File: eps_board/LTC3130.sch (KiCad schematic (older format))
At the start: 13 parts

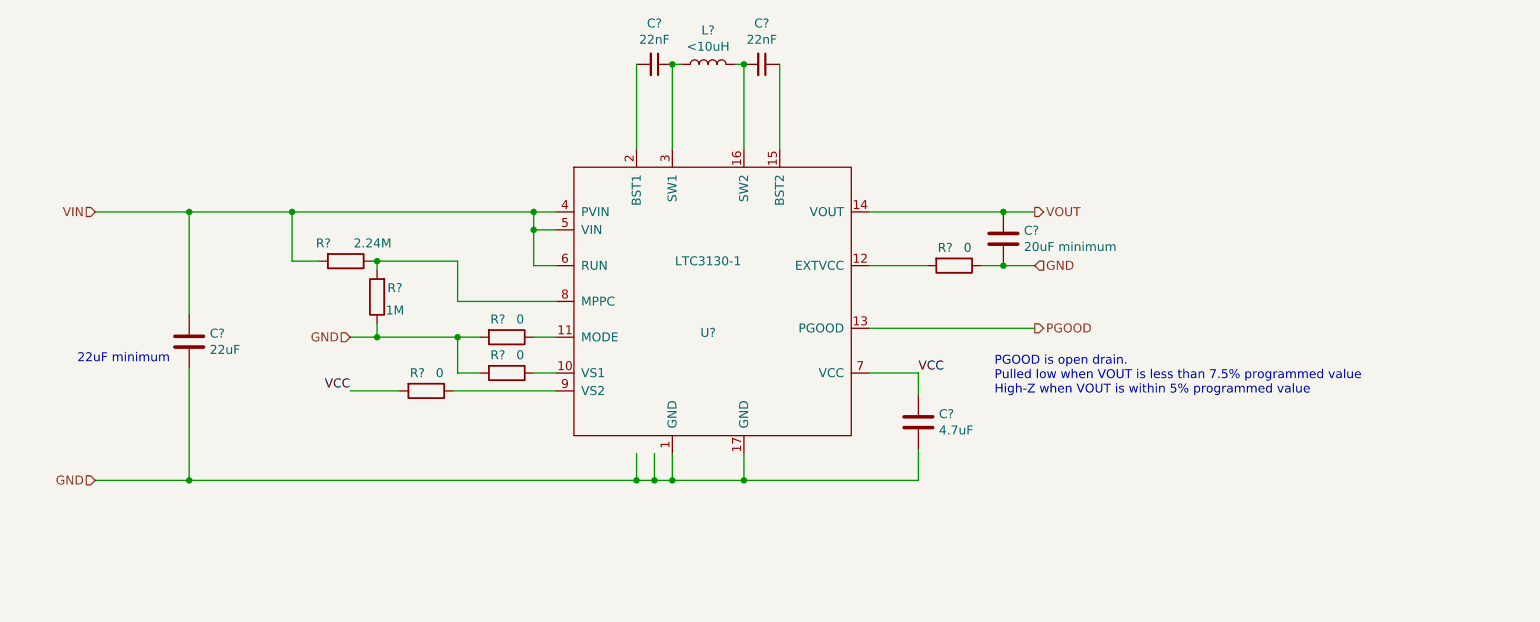
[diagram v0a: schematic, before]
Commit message: EPS with schottky diodes & 1 regulator
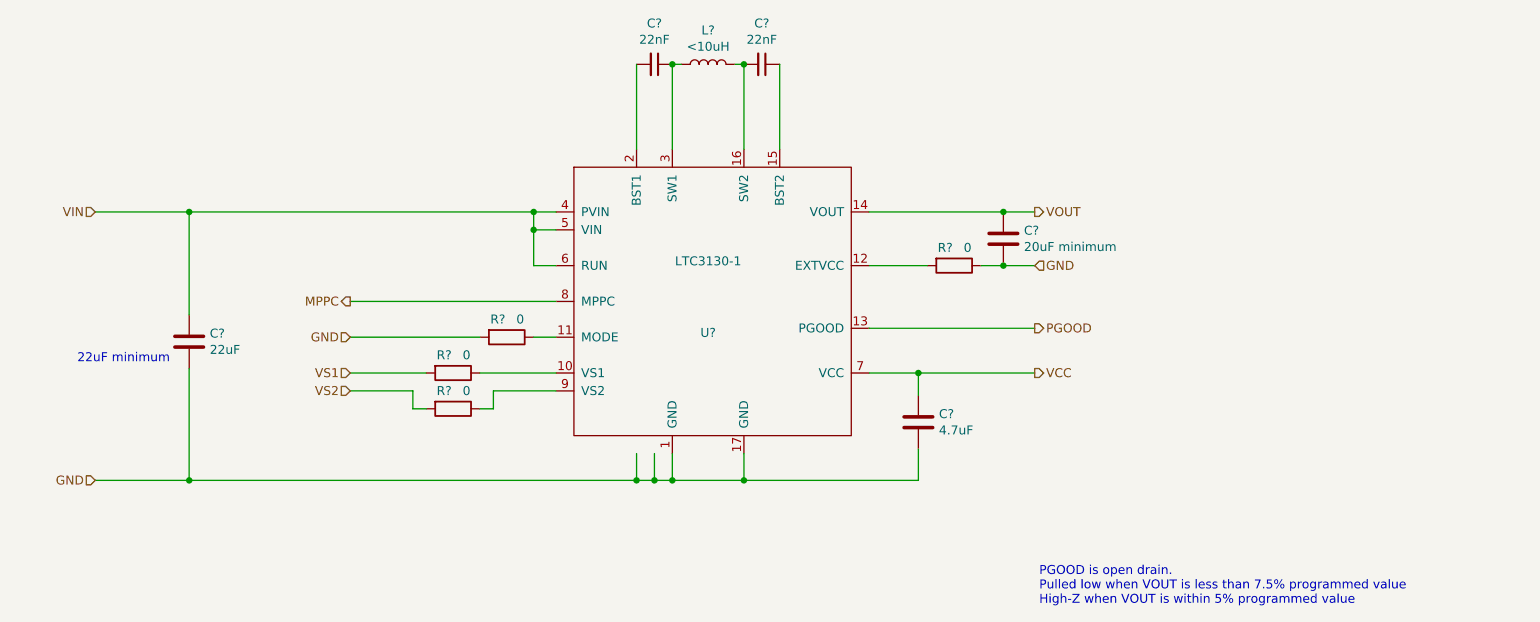
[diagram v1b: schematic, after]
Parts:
- removed R? (x2): 0, Resistor_SMD:R_0603_1608Metric_Pad1.05x0.95mm_HandSolder, symbol Device:R
- removed R?: 2.24M, Resistor_SMD:R_0603_1608Metric_Pad1.05x0.95mm_HandSolder, symbol Device:R
- removed R?: 1M, Resistor_SMD:R_0603_1608Metric_Pad1.05x0.95mm_HandSolder, symbol Device:R
- added R? (x2): 0, Resistor_SMD:R_0603_1608Metric_Pad1.05x0.95mm_HandSolder, symbol Device:R
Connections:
- net labels added: MPPC, VS1, VS2
- wire segments 52 -> 46
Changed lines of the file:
@@
 $Descr A 11000 8500
 encoding utf-8
-Sheet 10 21
+Sheet 14 14
 Title "SOLAR MPPT 5V BOOST"
 Date "2020-08-09"
@@
 EndData
 $EndBitmap
-Text Notes 6850 4350 0    50   ~ 0
+Text Notes 7100 5525 0    50   ~ 0
 PGOOD is open drain. \nPulled low when VOUT is less than 7.5% programmed value\nHigh-Z when VOUT is within 5% programmed value\n
 Text Notes 1725 4175 0    50   ~ 0
@@
 Wire Wire Line
 	2350 4200 2350 4825
-Wire Wire Line
-	2350 3325 2925 3325
 Connection ~ 2350 3325
 Wire Wire Line
@@
 AR Path="/5F355926/5F325818" Ref="C?"  Part="1"
 AR Path="/5F356470/5F325818" Ref="C?"  Part="1"
+AR Path="/5F52BDC8/5F325818" Ref="C?"  Part="1"
+AR Path="/5F5A5959/5F325818" Ref="C?"  Part="1"
+AR Path="/5F5C3BDB/5F325818" Ref="C?"  Part="1"
+AR Path="/5F62C305/5F325818" Ref="C?"  Part="1"
 F 0 "C?" H 2465 4096 50  0000 L CNN
 F 1 "22uF" H 2465 4005 50  0000 L CNN
@@
 $EndComp
 Wire Wire Line
-	3250 4325 3525 4325
-Text Label 3250 4325 2    50   ~ 0
-VCC
-Text Label 6425 4225 0    50   ~ 0
-VCC
-Wire Wire Line
-	2925 3325 4275 3325
-Connection ~ 2925 3325
-Wire Wire Line
-	2925 3600 3075 3600
-Wire Wire Line
-	2925 3325 2925 3600
-Wire Wire Line
 	1825 3325 2350 3325
 Text HLabel 1825 3325 0    50   Input ~ 0
 VIN
-Connection ~ 3400 3600
-Wire Wire Line
-	3850 3825 4400 3825
-Wire Wire Line
-	3850 3600 3850 3825
-Wire Wire Line
-	3400 3600 3850 3600
-Wire Wire Line
-	3400 3600 3400 3650
-Wire Wire Line
-	3375 3600 3400 3600
-Wire Wire Line
-	3400 4025 3850 4025
-Connection ~ 3400 4025
-Wire Wire Line
-	3400 3950 3400 4025
-Connection ~ 3850 4025
-Wire Wire Line
-	3250 4025 3400 4025
-$Comp
-L Device:R R?
-U 1 1 5F3185A7
-P 3400 3800
-AR Path="/5F301AC2/5F3185A7" Ref="R?"  Part="1"
-AR Path="/5F354B8C/5F3185A7" Ref="R?"  Part="1"
-AR Path="/5F354E2A/5F3185A7" Ref="R?"  Part="1"
-AR Path="/5F3552FC/5F3185A7" Ref="R?"  Part="1"
-AR Path="/5F355926/5F3185A7" Ref="R?"  Part="1"
-AR Path="/5F356470/5F3185A7" Ref="R?"  Part="1"
-F 0 "R?" H 3300 3750 50  0000 C CNN
-F 1 "1M" H 3300 3875 50  0000 C CNN
-F 2 "Resistor_SMD:R_0603_1608Metric_Pad1.05x0.95mm_HandSolder" V 3330 3800 50  0001 C CNN
-F 3 "~" H 3400 3800 50  0001 C CNN
-	1    3400 3800
-	-1   0    0    1
-$EndComp
-$Comp
-L Device:R R?
-U 1 1 5F318247
-P 3225 3600
-AR Path="/5F301AC2/5F318247" Ref="R?"  Part="1"
-AR Path="/5F354B8C/5F318247" Ref="R?"  Part="1"
-AR Path="/5F354E2A/5F318247" Ref="R?"  Part="1"
-AR Path="/5F3552FC/5F318247" Ref="R?"  Part="1"
-AR Path="/5F355926/5F318247" Ref="R?"  Part="1"
-AR Path="/5F356470/5F318247" Ref="R?"  Part="1"
-F 0 "R?" V 3125 3475 50  0000 C CNN
-F 1 "2.24M" V 3125 3750 50  0000 C CNN
-F 2 "Resistor_SMD:R_0603_1608Metric_Pad1.05x0.95mm_HandSolder" V 3155 3600 50  0001 C CNN
-F 3 "~" H 3225 3600 50  0001 C CNN
-	1    3225 3600
-	0    1    1    0
-$EndComp
-Wire Wire Line
-	3850 4225 3975 4225
-Wire Wire Line
-	3850 4025 3850 4225
-Wire Wire Line
-	3975 4025 3850 4025
 Wire Wire Line
 	4275 4025 4400 4025
@@
 AR Path="/5F355926/5F316C45" Ref="R?"  Part="1"
 AR Path="/5F356470/5F316C45" Ref="R?"  Part="1"
+AR Path="/5F52BDC8/5F316C45" Ref="R?"  Part="1"
+AR Path="/5F5A5959/5F316C45" Ref="R?"  Part="1"
+AR Path="/5F5C3BDB/5F316C45" Ref="R?"  Part="1"
+AR Path="/5F62C305/5F316C45" Ref="R?"  Part="1"
 F 0 "R?" V 4025 3975 50  0000 C CNN
 F 1 "0" V 4025 4100 50  0000 C CNN
@@
 AR Path="/5F355926/5F3159CA" Ref="R?"  Part="1"
 AR Path="/5F356470/5F3159CA" Ref="R?"  Part="1"
+AR Path="/5F52BDC8/5F3159CA" Ref="R?"  Part="1"
+AR Path="/5F5A5959/5F3159CA" Ref="R?"  Part="1"
+AR Path="/5F5C3BDB/5F3159CA" Ref="R?"  Part="1"
+AR Path="/5F62C305/5F3159CA" Ref="R?"  Part="1"
 F 0 "R?" V 6525 3575 50  0000 C CNN
 F 1 "0" V 6525 3700 50  0000 C CNN
@@
 	0    1    1    0
 $EndComp
-$Comp
-L Device:R R?
-U 1 1 5F31536B
-P 3675 4325
-AR Path="/5F301AC2/5F31536B" Ref="R?"  Part="1"
-AR Path="/5F354B8C/5F31536B" Ref="R?"  Part="1"
-AR Path="/5F354E2A/5F31536B" Ref="R?"  Part="1"
-AR Path="/5F3552FC/5F31536B" Ref="R?"  Part="1"
-AR Path="/5F355926/5F31536B" Ref="R?"  Part="1"
-AR Path="/5F356470/5F31536B" Ref="R?"  Part="1"
-F 0 "R?" V 3575 4275 50  0000 C CNN
-F 1 "0" V 3575 4400 50  0000 C CNN
-F 2 "Resistor_SMD:R_0603_1608Metric_Pad1.05x0.95mm_HandSolder" V 3605 4325 50  0001 C CNN
-F 3 "~" H 3675 4325 50  0001 C CNN
-	1    3675 4325
-	0    1    1    0
-$EndComp
-Wire Wire Line
-	4400 4325 3825 4325
-Wire Wire Line
-	4275 4225 4400 4225
-$Comp
-L Device:R R?
-U 1 1 5F313B85
-P 4125 4225
-AR Path="/5F301AC2/5F313B85" Ref="R?"  Part="1"
-AR Path="/5F354B8C/5F313B85" Ref="R?"  Part="1"
-AR Path="/5F354E2A/5F313B85" Ref="R?"  Part="1"
-AR Path="/5F3552FC/5F313B85" Ref="R?"  Part="1"
-AR Path="/5F355926/5F313B85" Ref="R?"  Part="1"
-AR Path="/5F356470/5F313B85" Ref="R?"  Part="1"
-F 0 "R?" V 4025 4175 50  0000 C CNN
-F 1 "0" V 4025 4300 50  0000 C CNN
-F 2 "Resistor_SMD:R_0603_1608Metric_Pad1.05x0.95mm_HandSolder" V 4055 4225 50  0001 C CNN
-F 3 "~" H 4125 4225 50  0001 C CNN
-	1    4125 4225
-	0    1    1    0
-$EndComp
 Text HLabel 3250 4025 0    50   Input ~ 0
 GND
@@
 AR Path="/5F355926/5F30F8B8" Ref="C?"  Part="1"
 AR Path="/5F356470/5F30F8B8" Ref="C?"  Part="1"
+AR Path="/5F52BDC8/5F30F8B8" Ref="C?"  Part="1"
+AR Path="/5F5A5959/5F30F8B8" Ref="C?"  Part="1"
+AR Path="/5F5C3BDB/5F30F8B8" Ref="C?"  Part="1"
+AR Path="/5F62C305/5F30F8B8" Ref="C?"  Part="1"
 F 0 "C?" H 7015 3521 50  0000 L CNN
 F 1 "20uF minimum" H 7015 3430 50  0000 L CNN
@@
 AR Path="/5F355926/5F30F29C" Ref="C?"  Part="1"
 AR Path="/5F356470/5F30F29C" Ref="C?"  Part="1"
+AR Path="/5F52BDC8/5F30F29C" Ref="C?"  Part="1"
+AR Path="/5F5A5959/5F30F29C" Ref="C?"  Part="1"
+AR Path="/5F5C3BDB/5F30F29C" Ref="C?"  Part="1"
+AR Path="/5F62C305/5F30F29C" Ref="C?"  Part="1"
 F 0 "C?" V 5321 2500 50  0000 C CNN
 F 1 "22nF" V 5412 2500 50  0000 C CNN
@@
 AR Path="/5F355926/5F30E2F4" Ref="C?"  Part="1"
 AR Path="/5F356470/5F30E2F4" Ref="C?"  Part="1"
+AR Path="/5F52BDC8/5F30E2F4" Ref="C?"  Part="1"
+AR Path="/5F5A5959/5F30E2F4" Ref="C?"  Part="1"
+AR Path="/5F5C3BDB/5F30E2F4" Ref="C?"  Part="1"
+AR Path="/5F62C305/5F30E2F4" Ref="C?"  Part="1"
 F 0 "C?" V 4721 2500 50  0000 C CNN
 F 1 "22nF" V 4812 2500 50  0000 C CNN
@@
 AR Path="/5F355926/5F30C7DB" Ref="L?"  Part="1"
 AR Path="/5F356470/5F30C7DB" Ref="L?"  Part="1"
+AR Path="/5F52BDC8/5F30C7DB" Ref="L?"  Part="1"
+AR Path="/5F5A5959/5F30C7DB" Ref="L?"  Part="1"
+AR Path="/5F5C3BDB/5F30C7DB" Ref="L?"  Part="1"
+AR Path="/5F62C305/5F30C7DB" Ref="L?"  Part="1"
 F 0 "L?" V 5440 2500 50  0000 C CNN
 F 1 "<10uH" V 5349 2500 50  0000 C CNN
@@
 AR Path="/5F355926/5F30A62E" Ref="C?"  Part="1"
 AR Path="/5F356470/5F30A62E" Ref="C?"  Part="1"
+AR Path="/5F52BDC8/5F30A62E" Ref="C?"  Part="1"
+AR Path="/5F5A5959/5F30A62E" Ref="C?"  Part="1"
+AR Path="/5F5C3BDB/5F30A62E" Ref="C?"  Part="1"
+AR Path="/5F62C305/5F30A62E" Ref="C?"  Part="1"
 F 0 "C?" H 6540 4546 50  0000 L CNN
 F 1 "4.7uF" H 6540 4455 50  0000 L CNN
@@
 AR Path="/5F355926/5F30989D" Ref="U?"  Part="1"
 AR Path="/5F356470/5F30989D" Ref="U?"  Part="1"
+AR Path="/5F52BDC8/5F30989D" Ref="U?"  Part="1"
+AR Path="/5F5A5959/5F30989D" Ref="U?"  Part="1"
+AR Path="/5F5C3BDB/5F30989D" Ref="U?"  Part="1"
+AR Path="/5F62C305/5F30989D" Ref="U?"  Part="1"
 F 0 "U?" H 5250 3650 50  0000 C CNN
 F 1 "LTC3130-1" H 5250 4050 50  0000 C CNN
@@
 Wire Wire Line
 	4950 4825 5050 4825
+Text HLabel 7075 4225 2    50   Output ~ 0
+VCC
+Wire Wire Line
+	7075 4225 6425 4225
+Connection ~ 6425 4225
+Text HLabel 3250 4225 0    50   Input ~ 0
+VS1
+Text HLabel 3250 4325 0    50   Input ~ 0
+VS2
+$Comp
+L Device:R R?
+U 1 1 5F5775AC
+P 3825 4425
+AR Path="/5F301AC2/5F5775AC" Ref="R?"  Part="1"
+AR Path="/5F354B8C/5F5775AC" Ref="R?"  Part="1"
+AR Path="/5F354E2A/5F5775AC" Ref="R?"  Part="1"
+AR Path="/5F3552FC/5F5775AC" Ref="R?"  Part="1"
+AR Path="/5F355926/5F5775AC" Ref="R?"  Part="1"
+AR Path="/5F356470/5F5775AC" Ref="R?"  Part="1"
+AR Path="/5F52BDC8/5F5775AC" Ref="R?"  Part="1"
+AR Path="/5F5775AC" Ref="R?"  Part="1"
+AR Path="/5F5A5959/5F5775AC" Ref="R?"  Part="1"
+AR Path="/5F5C3BDB/5F5775AC" Ref="R?"  Part="1"
+AR Path="/5F62C305/5F5775AC" Ref="R?"  Part="1"
+F 0 "R?" V 3725 4375 50  0000 C CNN
+F 1 "0" V 3725 4500 50  0000 C CNN
+F 2 "Resistor_SMD:R_0603_1608Metric_Pad1.05x0.95mm_HandSolder" V 3755 4425 50  0001 C CNN
+F 3 "~" H 3825 4425 50  0001 C CNN
+	1    3825 4425
+	0    1    1    0
+$EndComp
+$Comp
+L Device:R R?
+U 1 1 5F5775B2
+P 3825 4225
+AR Path="/5F301AC2/5F5775B2" Ref="R?"  Part="1"
+AR Path="/5F354B8C/5F5775B2" Ref="R?"  Part="1"
+AR Path="/5F354E2A/5F5775B2" Ref="R?"  Part="1"
+AR Path="/5F3552FC/5F5775B2" Ref="R?"  Part="1"
+AR Path="/5F355926/5F5775B2" Ref="R?"  Part="1"
+AR Path="/5F356470/5F5775B2" Ref="R?"  Part="1"
+AR Path="/5F52BDC8/5F5775B2" Ref="R?"  Part="1"
+AR Path="/5F5775B2" Ref="R?"  Part="1"
+AR Path="/5F5A5959/5F5775B2" Ref="R?"  Part="1"
+AR Path="/5F5C3BDB/5F5775B2" Ref="R?"  Part="1"
+AR Path="/5F62C305/5F5775B2" Ref="R?"  Part="1"
+F 0 "R?" V 3725 4175 50  0000 C CNN
+F 1 "0" V 3725 4300 50  0000 C CNN
+F 2 "Resistor_SMD:R_0603_1608Metric_Pad1.05x0.95mm_HandSolder" V 3755 4225 50  0001 C CNN
+F 3 "~" H 3825 4225 50  0001 C CNN
+	1    3825 4225
+	0    1    1    0
+$EndComp
+Wire Wire Line
+	3975 4225 4400 4225
+Wire Wire Line
+	3675 4225 3250 4225
+Wire Wire Line
+	3975 4425 4050 4425
+Wire Wire Line
+	4050 4425 4050 4325
+Wire Wire Line
+	4050 4325 4400 4325
+Wire Wire Line
+	3675 4425 3600 4425
+Wire Wire Line
+	3600 4425 3600 4325
+Wire Wire Line
+	3600 4325 3250 4325
+Text HLabel 3250 3825 0    50   Output ~ 0
+MPPC
+Wire Wire Line
+	3250 3825 4400 3825
+Wire Wire Line
+	3250 4025 3975 4025
+Wire Wire Line
+	2350 3325 4275 3325
 $EndSCHEMATC

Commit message: Progress on EPS
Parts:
- removed C?: 22nF, Capacitor_SMD:C_0603_1608Metric_Pad1.05x0.95mm_HandSolder, symbol Device:C_Small
- added C?: 22nF, Capacitor_SMD:C_0603_1608Metric_Pad1.05x0.95mm_HandSolder, symbol Device:C_Small
- added C?: DNP, Capacitor_SMD:C_1210_3225Metric_Pad1.42x2.65mm_HandSolder, symbol Device:C
- added C?: DNP, Capacitor_SMD:C_0603_1608Metric_Pad1.05x0.95mm_HandSolder, symbol Device:C
- added C?: 1uF, Capacitor_SMD:C_0603_1608Metric_Pad1.05x0.95mm_HandSolder, symbol Device:C
- added C?: 47uF, Capacitor_SMD:C_1210_3225Metric_Pad1.42x2.65mm_HandSolder, symbol Device:C
- C?: Mfr. # (none) -> GCM188R72A223KA37D; Order (none) -> https://www.digikey.com/product-detail/en/murata-electronic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
- C?: value 20uF minimum -> 47uF; footprint Capacitor_SMD:C_0603_1608Metric_Pad1.05x0.95mm_HandSolder -> Capacitor_SMD:C_1210_3225Metric_Pad1.42x2.65mm_HandSolder; Mfr. # (none) -> GRM32EC81C476KE15L; Order (none) -> https://www.digikey.com/product-detail/en/murata-electronic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
- C?: value 22uF -> 4.7uF
- L?: value <10uH -> 4.7uH; footprint (none) -> Inductor_SMD:L_Coilcraft_LPS4018; Mfr. # (none) -> LPS4018-472; Order (none) -> https://www.coilcraft.com/en-us/products/power/shielded-ind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
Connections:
- wire segments 46 -> 57
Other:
- note removed: "22uF minimum\n"
- moved on the sheet: C?, R?

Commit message: Essentially done with EPS schematic
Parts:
- removed U?: LTC3130-1, Package_SO:MSOP-16-1EP_3x4.039mm_P0.5mm_EP1.651x2.845mm_ThermalVias, symbol 1K_Custom_Symbol:LTC3130-1
- added U83: LTC3130-1, Package_SO:MSOP-16-1EP_3x4.039mm_P0.5mm_EP1.651x2.845mm_ThermalVias, symbol 1K_Custom_Symbol:LTC3130-1
- C32, C41: renamed from C?; Voltage (none) -> 16V
- C33, C40: renamed from C?; Mfr. # (none) -> C1608X7S1A475K080AC; Order (none) -> https://www.digikey.com/product-detail/en/tdk-corporation/C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; Voltage (none) -> 10V
- C34: renamed from C?; Mfr. # (none) -> CL10B105KP8NFNC; Order (none) -> https://www.digikey.com/product-detail/en/samsung-electro-m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; Voltage (none) -> 10V
- C35, C37: renamed from C?; Voltage (none) -> 100V
- C42, C43: renamed from C?; Mfr. # GRM32EC81C476KE15L -> (none); Order https://www.digikey.com/product-detail/en/murata-electronic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 -> (none)
- R87, R88, R89, R90: renamed from R?; Mfr. # (none) -> RK73Z1JTTD; Order (none) -> https://www.digikey.com/product-detail/en/koa-speer-electro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
- gave numbers to parts that had none: 1
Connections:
- wire segments 57 -> 63
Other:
- moved on the sheet: C177, C178, R318

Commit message: EPS layout in progress
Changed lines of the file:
@@
 $Descr A 11000 8500
 encoding utf-8
-Sheet 39 39
+Sheet 8 39
 Title "LTC3130"
 Date "2020-08-09"
@@
 AR Path="/5F62C305/5F325818" Ref="C?"  Part="1"
 AR Path="/5FCD393E/5F325818" Ref="C175"  Part="1"
-F 0 "C175" H 2375 3625 50  0000 L CNN
+F 0 "C33" H 2375 3625 50  0000 L CNN
 F 1 "4.7uF" H 2375 3550 50  0000 L CNN
 F 2 "Capacitor_SMD:C_0603_1608Metric_Pad1.05x0.95mm_HandSolder" H 2313 3425 50  0001 C CNN
@@
 AR Path="/5F62C305/5F316C45" Ref="R?"  Part="1"
 AR Path="/5FCD393E/5F316C45" Ref="R318"  Part="1"
-F 0 "R318" V 3725 3975 50  0000 C CNN
+F 0 "R89" V 3725 3975 50  0000 C CNN
 F 1 "0" V 3725 4100 50  0000 C CNN
 F 2 "Resistor_SMD:R_0603_1608Metric_Pad1.05x0.95mm_HandSolder" V 3755 4025 50  0001 C CNN
@@
 AR Path="/5F62C305/5F3159CA" Ref="R?"  Part="1"
 AR Path="/5FCD393E/5F3159CA" Ref="R319"  Part="1"
-F 0 "R319" V 6350 3575 50  0000 C CNN
+F 0 "R90" V 6350 3575 50  0000 C CNN
 F 1 "0" V 6350 3700 50  0000 C CNN
 F 2 "Resistor_SMD:R_0603_1608Metric_Pad1.05x0.95mm_HandSolder" V 6380 3625 50  0001 C CNN
@@
 AR Path="/5F62C305/5F30F8B8" Ref="C?"  Part="1"
 AR Path="/5FCD393E/5F30F8B8" Ref="C180"  Part="1"
-F 0 "C180" H 6900 3550 50  0000 L CNN
+F 0 "C41" H 6900 3550 50  0000 L CNN
 F 1 "47uF" H 6900 3475 50  0000 L CNN
 F 2 "Capacitor_SMD:C_1210_3225Metric_Pad1.42x2.65mm_HandSolder" H 6838 3325 50  0001 C CNN
@@
 AR Path="/5F62C305/5F30E2F4" Ref="C?"  Part="1"
 AR Path="/5FCD393E/5F30E2F4" Ref="C177"  Part="1"
-F 0 "C177" V 4521 2500 50  0000 C CNN
+F 0 "C35" V 4521 2500 50  0000 C CNN
 F 1 "22nF" V 4612 2500 50  0000 C CNN
 F 2 "Capacitor_SMD:C_0603_1608Metric_Pad1.05x0.95mm_HandSolder" H 4750 2500 50  0001 C CNN
@@
 AR Path="/5F62C305/5F30C7DB" Ref="L?"  Part="1"
 AR Path="/5FCD393E/5F30C7DB" Ref="L2"  Part="1"
-F 0 "L2" V 5400 2500 50  0000 C CNN
+F 0 "L1" V 5400 2500 50  0000 C CNN
 F 1 "4.7uH" V 5325 2500 50  0000 C CNN
 F 2 "Inductor_SMD:L_Coilcraft_LPS4018" H 5250 2500 50  0001 C CNN
@@
 AR Path="/5F62C305/5F30A62E" Ref="C?"  Part="1"
 AR Path="/5FCD393E/5F30A62E" Ref="C179"  Part="1"
-F 0 "C179" H 6525 4550 50  0000 L CNN
+F 0 "C40" H 6525 4550 50  0000 L CNN
 F 1 "4.7uF" H 6525 4475 50  0000 L CNN
 F 2 "Capacitor_SMD:C_0603_1608Metric_Pad1.05x0.95mm_HandSolder" H 6463 4350 50  0001 C CNN
@@
 AR Path="/5F62C305/5F5775AC" Ref="R?"  Part="1"
 AR Path="/5FCD393E/5F5775AC" Ref="R317"  Part="1"
-F 0 "R317" V 3725 4375 50  0000 C CNN
+F 0 "R88" V 3725 4375 50  0000 C CNN
 F 1 "0" V 3725 4500 50  0000 C CNN
 F 2 "Resistor_SMD:R_0603_1608Metric_Pad1.05x0.95mm_HandSolder" V 3755 4425 50  0001 C CNN
@@
 AR Path="/5F62C305/5F5775B2" Ref="R?"  Part="1"
 AR Path="/5FCD393E/5F5775B2" Ref="R316"  Part="1"
-F 0 "R316" V 3725 4175 50  0000 C CNN
+F 0 "R87" V 3725 4175 50  0000 C CNN
 F 1 "0" V 3725 4300 50  0000 C CNN
 F 2 "Resistor_SMD:R_0603_1608Metric_Pad1.05x0.95mm_HandSolder" V 3755 4225 50  0001 C CNN
@@
 AR Path="/5F62C305/5F915D60" Ref="C?"  Part="1"
 AR Path="/5FCD393E/5F915D60" Ref="C178"  Part="1"
-F 0 "C178" V 5525 2500 50  0000 C CNN
+F 0 "C37" V 5525 2500 50  0000 C CNN
 F 1 "22nF" V 5600 2500 50  0000 C CNN
 F 2 "Capacitor_SMD:C_0603_1608Metric_Pad1.05x0.95mm_HandSolder" H 5750 2500 50  0001 C CNN
@@
 AR Path="/5F62C305/5F918110" Ref="C?"  Part="1"
 AR Path="/5FCD393E/5F918110" Ref="C181"  Part="1"
-F 0 "C181" H 7365 3521 50  0000 L CNN
+F 0 "C42" H 7365 3521 50  0000 L CNN
 F 1 "DNP" H 7365 3430 50  0000 L CNN
 F 2 "Capacitor_SMD:C_1210_3225Metric_Pad1.42x2.65mm_HandSolder" H 7288 3325 50  0001 C CNN
@@
 AR Path="/5F62C305/5F91837D" Ref="C?"  Part="1"
 AR Path="/5FCD393E/5F91837D" Ref="C182"  Part="1"
-F 0 "C182" H 7815 3521 50  0000 L CNN
+F 0 "C43" H 7815 3521 50  0000 L CNN
 F 1 "DNP" H 7815 3430 50  0000 L CNN
 F 2 "Capacitor_SMD:C_0603_1608Metric_Pad1.05x0.95mm_HandSolder" H 7738 3325 50  0001 C CNN
@@
 AR Path="/5F62C305/5F91FDED" Ref="C?"  Part="1"
 AR Path="/5FCD393E/5F91FDED" Ref="C176"  Part="1"
-F 0 "C176" H 2825 3625 50  0000 L CNN
+F 0 "C34" H 2825 3625 50  0000 L CNN
 F 1 "1uF" H 2825 3550 50  0000 L CNN
 F 2 "Capacitor_SMD:C_0603_1608Metric_Pad1.05x0.95mm_HandSolder" H 2763 3425 50  0001 C CNN
@@
 AR Path="/5F62C305/5F92B281" Ref="C?"  Part="1"
 AR Path="/5FCD393E/5F92B281" Ref="C174"  Part="1"
-F 0 "C174" H 1925 3625 50  0000 L CNN
+F 0 "C32" H 1925 3625 50  0000 L CNN
 F 1 "47uF" H 1925 3550 50  0000 L CNN
 F 2 "Capacitor_SMD:C_1210_3225Metric_Pad1.42x2.65mm_HandSolder" H 1863 3425 50  0001 C CNN
@@
 AR Path="/5FCD393E/638BE07D" Ref="U83"  Part="1"
 AR Path="/5F301AC2/638BE07D" Ref="U16"  Part="1"
-F 0 "U83" H 5275 3825 50  0000 C CNN
+AR Path="/638BE07D" Ref="U83"  Part="1"
+F 0 "U16" H 5275 3825 50  0000 C CNN
 F 1 "LTC3130-1" H 5250 3425 50  0000 C CNN
 F 2 "Package_SO:MSOP-16-1EP_3x4.039mm_P0.5mm_EP1.651x2.845mm_ThermalVias" H 5300 2575 50  0001 C CNN
